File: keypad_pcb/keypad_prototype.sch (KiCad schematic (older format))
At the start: 31 parts, among them U1 KEYPAD_OVERLAY

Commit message: New keypad PCB
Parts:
- C1, C2, C3, C4, C5, C6, GREEN1, RED1: footprint Buttons_Switches_SMD:SW_SPST_EVQPE1 -> footprints:SW_SPST_EVQPE1
- OPTION1, PHOTO1, PHOTO2, VOL_DOWN1, VOL_UP1: footprint Buttons_Switches_SMD:SW_SPST_EVQP7C -> footprints:SW_SPST_EVQP7C
- U1: footprint keypad_overlay:KEYPAD_OVERLAY -> (none)
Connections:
- no-connect marks 2 -> 7
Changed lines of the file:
@@
 LIBS:valves
 LIBS:keypad_overlay
-LIBS:ab2_input_devices
 LIBS:keypad_prototype-cache
 EELAYER 25 0
@@
 $EndDescr
 $Comp
-L KEYPAD_OVERLAY U1
-U 1 1 58471DAF
-P 3650 2100
-F 0 "U1" H 3100 1450 60  0000 C CNN
-F 1 "KEYPAD_OVERLAY" H 3450 2500 60  0000 C CNN
-F 2 "keypad_overlay:KEYPAD_OVERLAY" H 3650 2100 60  0001 C CNN
-F 3 "" H 3650 2100 60  0001 C CNN
-	1    3650 2100
-	1    0    0    -1
-$EndComp
-$Comp
 L AB2_SWITCH_MOMENTARY VOL_DOWN1
 U 1 1 58471E29
@@
 F 0 "VOL_DOWN1" H 2650 3450 60  0000 C CNN
 F 1 "AB2_SWITCH_MOMENTARY" H 2650 3650 60  0001 C CNN
-F 2 "Buttons_Switches_SMD:SW_SPST_EVQP7C" H 2650 3500 60  0001 C CNN
+F 2 "footprints:SW_SPST_EVQP7C" H 2650 3500 60  0001 C CNN
 F 3 "" H 2650 3500 60  0000 C CNN
 	1    2650 3500
@@
 F 0 "VOL_UP1" H 3200 3450 60  0000 C CNN
 F 1 "AB2_SWITCH_MOMENTARY" H 3200 3650 60  0001 C CNN
-F 2 "Buttons_Switches_SMD:SW_SPST_EVQP7C" H 3200 3500 60  0001 C CNN
+F 2 "footprints:SW_SPST_EVQP7C" H 3200 3500 60  0001 C CNN
 F 3 "" H 3200 3500 60  0000 C CNN
 	1    3200 3500
@@
 F 0 "C1" H 3750 3450 60  0000 C CNN
 F 1 "AB2_SWITCH_MOMENTARY" H 3750 3650 60  0001 C CNN
-F 2 "Buttons_Switches_SMD:SW_SPST_EVQPE1" H 3750 3500 60  0001 C CNN
+F 2 "footprints:SW_SPST_EVQPE1" H 3750 3500 60  0001 C CNN
 F 3 "" H 3750 3500 60  0000 C CNN
 	1    3750 3500
@@
 F 0 "C2" H 4850 3450 60  0000 C CNN
 F 1 "AB2_SWITCH_MOMENTARY" H 4850 3650 60  0001 C CNN
-F 2 "Buttons_Switches_SMD:SW_SPST_EVQPE1" H 4850 3500 60  0001 C CNN
+F 2 "footprints:SW_SPST_EVQPE1" H 4850 3500 60  0001 C CNN
 F 3 "" H 4850 3500 60  0000 C CNN
 	1    4850 3500
@@
 F 0 "GREEN1" H 2650 3800 60  0000 C CNN
 F 1 "AB2_SWITCH_MOMENTARY" H 2650 4000 60  0001 C CNN
-F 2 "Buttons_Switches_SMD:SW_SPST_EVQPE1" H 2650 3850 60  0001 C CNN
+F 2 "footprints:SW_SPST_EVQPE1" H 2650 3850 60  0001 C CNN
 F 3 "" H 2650 3850 60  0000 C CNN
 	1    2650 3850
@@
 F 0 "RED1" H 4850 3800 60  0000 C CNN
 F 1 "AB2_SWITCH_MOMENTARY" H 4850 4000 60  0001 C CNN
-F 2 "Buttons_Switches_SMD:SW_SPST_EVQPE1" H 4850 3850 60  0001 C CNN
+F 2 "footprints:SW_SPST_EVQPE1" H 4850 3850 60  0001 C CNN
 F 3 "" H 4850 3850 60  0000 C CNN
 	1    4850 3850
@@
 F 0 "C3" H 3200 4150 60  0000 C CNN
 F 1 "AB2_SWITCH_MOMENTARY" H 3200 4350 60  0001 C CNN
-F 2 "Buttons_Switches_SMD:SW_SPST_EVQPE1" H 3200 4200 60  0001 C CNN
+F 2 "footprints:SW_SPST_EVQPE1" H 3200 4200 60  0001 C CNN
 F 3 "" H 3200 4200 60  0000 C CNN
 	1    3200 4200
@@
 F 0 "C4" H 4300 4150 60  0000 C CNN
 F 1 "AB2_SWITCH_MOMENTARY" H 4300 4350 60  0001 C CNN
-F 2 "Buttons_Switches_SMD:SW_SPST_EVQPE1" H 4300 4200 60  0001 C CNN
+F 2 "footprints:SW_SPST_EVQPE1" H 4300 4200 60  0001 C CNN
 F 3 "" H 4300 4200 60  0000 C CNN
 	1    4300 4200
@@
 F 0 "OPTION1" H 2650 4800 60  0000 C CNN
 F 1 "AB2_SWITCH_MOMENTARY" H 2650 5000 60  0001 C CNN
-F 2 "Buttons_Switches_SMD:SW_SPST_EVQP7C" H 2650 4850 60  0001 C CNN
+F 2 "footprints:SW_SPST_EVQP7C" H 2650 4850 60  0001 C CNN
 F 3 "" H 2650 4850 60  0000 C CNN
 	1    2650 4850
@@
 F 0 "PHOTO1" H 4850 4800 60  0000 C CNN
 F 1 "AB2_SWITCH_MOMENTARY" H 4850 5000 60  0001 C CNN
-F 2 "Buttons_Switches_SMD:SW_SPST_EVQP7C" H 4850 4850 60  0001 C CNN
+F 2 "footprints:SW_SPST_EVQP7C" H 4850 4850 60  0001 C CNN
 F 3 "" H 4850 4850 60  0000 C CNN
 	1    4850 4850
@@
 F 0 "C5" H 2650 5150 60  0000 C CNN
 F 1 "AB2_SWITCH_MOMENTARY" H 2650 5350 60  0001 C CNN
-F 2 "Buttons_Switches_SMD:SW_SPST_EVQPE1" H 2650 5200 60  0001 C CNN
+F 2 "footprints:SW_SPST_EVQPE1" H 2650 5200 60  0001 C CNN
 F 3 "" H 2650 5200 60  0000 C CNN
 	1    2650 5200
@@
 F 0 "C6" H 4300 5150 60  0000 C CNN
 F 1 "AB2_SWITCH_MOMENTARY" H 4300 5350 60  0001 C CNN
-F 2 "Buttons_Switches_SMD:SW_SPST_EVQPE1" H 4300 5200 60  0001 C CNN
+F 2 "footprints:SW_SPST_EVQPE1" H 4300 5200 60  0001 C CNN
 F 3 "" H 4300 5200 60  0000 C CNN
 	1    4300 5200
@@
 F 0 "PHOTO2" H 4850 5150 60  0000 C CNN
 F 1 "AB2_SWITCH_MOMENTARY" H 4850 5350 60  0001 C CNN
-F 2 "Buttons_Switches_SMD:SW_SPST_EVQP7C" H 4850 5200 60  0001 C CNN
+F 2 "footprints:SW_SPST_EVQP7C" H 4850 5200 60  0001 C CNN
 F 3 "" H 4850 5200 60  0000 C CNN
 	1    4850 5200
@@
 NoConn ~ 2850 2450
 NoConn ~ 2850 2550
+$Comp
+L KEYPAD_OVERLAY U1
+U 1 1 58866251
+P 3650 2100
+F 0 "U1" H 3100 1450 60  0000 C CNN
+F 1 "KEYPAD_OVERLAY" H 3450 2500 60  0000 C CNN
+F 2 "" H 3650 2100 60  0001 C CNN
+F 3 "" H 3650 2100 60  0001 C CNN
+	1    3650 2100
+	1    0    0    -1
+$EndComp
+NoConn ~ 3350 2850
+NoConn ~ 3450 2850
+NoConn ~ 3550 2850
+NoConn ~ 3650 2850
+NoConn ~ 3750 2850
 $EndSCHEMATC

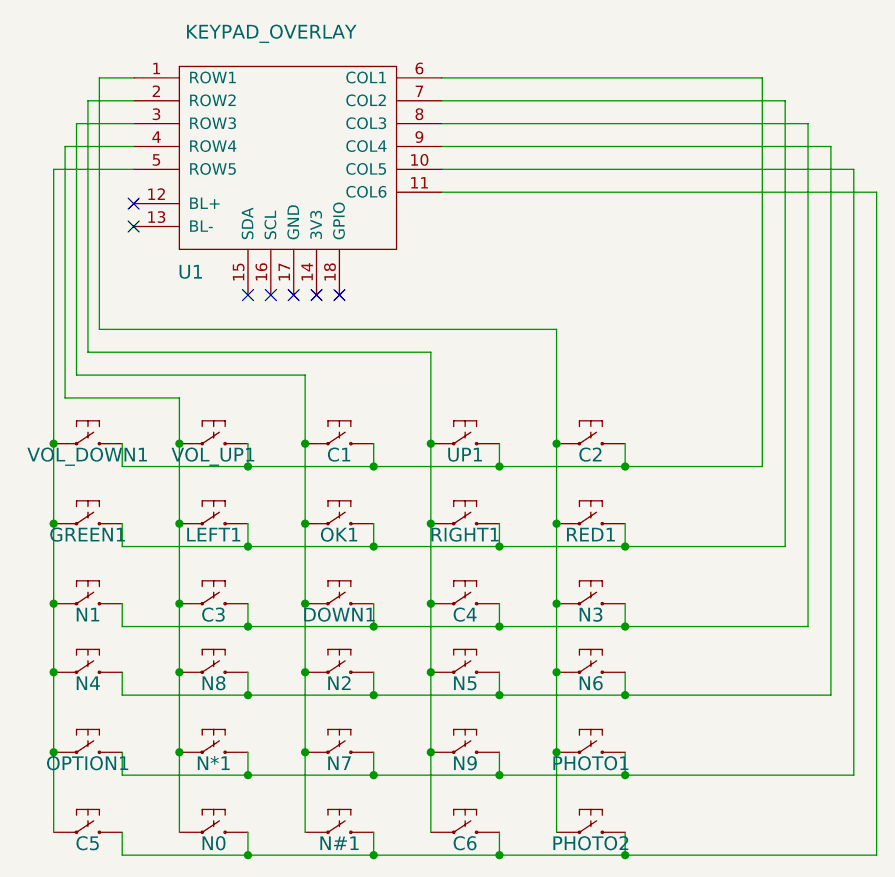
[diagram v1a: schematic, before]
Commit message: Silkscreen additions for keypad board
-Notes on soldering
-Tips for soldering
-Pin names
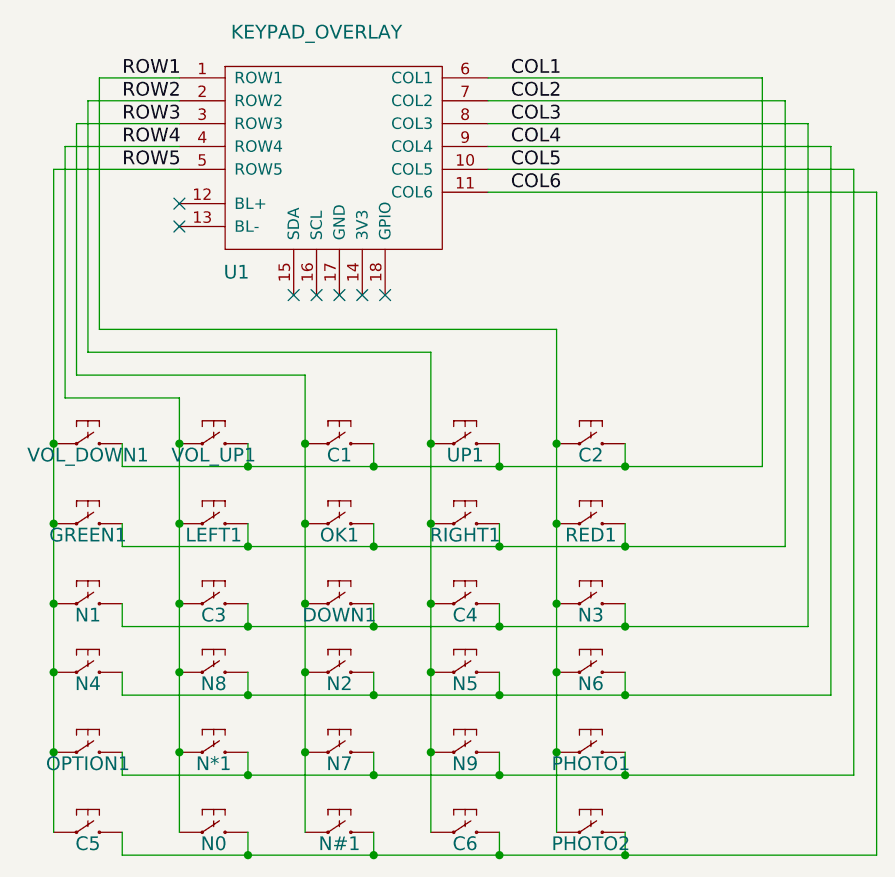
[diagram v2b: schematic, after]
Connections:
- net ROW5: now reaches C5.1, GREEN1.1, N1.1, N4.1, OPTION1.1, U1.5 (ROW5), VOL_DOWN1.1
- net COL1: now reaches C1.2, C2.2, U1.6 (COL1), UP1.2, VOL_DOWN1.2, VOL_UP1.2
- net ROW4: now reaches C3.1, LEFT1.1, N*1.1, N0.1, N8.1, U1.4 (ROW4), VOL_UP1.1
- net ROW3: now reaches C1.1, DOWN1.1, N#1.1, N2.1, N7.1, OK1.1, U1.3 (ROW3)
- net ROW2: now reaches C4.1, C6.1, N5.1, N9.1, RIGHT1.1, U1.2 (ROW2), UP1.1
- net ROW1: now reaches C2.1, N3.1, N6.1, PHOTO1.1, PHOTO2.1, RED1.1, U1.1 (ROW1)
- net COL2: now reaches GREEN1.2, LEFT1.2, OK1.2, RED1.2, RIGHT1.2, U1.7 (COL2)
- net COL3: now reaches C3.2, C4.2, DOWN1.2, N1.2, N3.2, U1.8 (COL3)
- net COL4: now reaches N2.2, N4.2, N5.2, N6.2, N8.2, U1.9 (COL4)
- net COL5: now reaches N*1.2, N7.2, N9.2, OPTION1.2, PHOTO1.2, U1.10 (COL5)
- net COL6: now reaches C5.2, C6.2, N#1.2, N0.2, PHOTO2.2, U1.11 (COL6)
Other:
- moved on the sheet: U1
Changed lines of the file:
@@
 	2500 2300 2500 5200
 Wire Wire Line
-	2700 1900 2850 1900
+	2700 1900 3050 1900
 Wire Wire Line
 	2700 1900 2700 3000
 Wire Wire Line
-	2850 2000 2650 2000
+	2650 2000 3050 2000
 Wire Wire Line
 	2650 2000 2650 3100
 Wire Wire Line
-	2850 2100 2600 2100
+	2600 2100 3050 2100
 Wire Wire Line
 	2600 2100 2600 3200
 Wire Wire Line
-	2850 2200 2550 2200
+	2550 2200 3050 2200
 Wire Wire Line
 	2550 2200 2550 3300
 Wire Wire Line
-	2850 2300 2500 2300
+	2500 2300 3050 2300
 Wire Wire Line
-	4200 2400 6100 2400
-Wire Wire Line
-	6100 2400 6100 5300
+	6100 5300 6100 2400
 Wire Wire Line
 	6000 4950 6000 2300
 Wire Wire Line
-	6000 2300 4200 2300
-Wire Wire Line
-	4200 2200 5900 2200
-Wire Wire Line
-	5900 2200 5900 4600
+	5900 4600 5900 2200
 Wire Wire Line
 	5800 4300 5800 2100
 Wire Wire Line
-	5800 2100 4200 2100
-Wire Wire Line
-	4200 2000 5700 2000
-Wire Wire Line
-	5700 2000 5700 3950
+	5700 3950 5700 2000
 Wire Wire Line
 	5600 3600 5600 1900
-Wire Wire Line
-	5600 1900 4200 1900
-NoConn ~ 2850 2450
-NoConn ~ 2850 2550
+NoConn ~ 3050 2450
+NoConn ~ 3050 2550
 $Comp
 L KEYPAD_OVERLAY U1
 U 1 1 58866251
-P 3650 2100
-F 0 "U1" H 3100 1450 60  0000 C CNN
-F 1 "KEYPAD_OVERLAY" H 3450 2500 60  0000 C CNN
-F 2 "" H 3650 2100 60  0001 C CNN
-F 3 "" H 3650 2100 60  0001 C CNN
-	1    3650 2100
+P 3850 2100
+F 0 "U1" H 3300 1450 60  0000 C CNN
+F 1 "KEYPAD_OVERLAY" H 3650 2500 60  0000 C CNN
+F 2 "" H 3850 2100 60  0001 C CNN
+F 3 "" H 3850 2100 60  0001 C CNN
+	1    3850 2100
 	1    0    0    -1
 $EndComp
-NoConn ~ 3350 2850
-NoConn ~ 3450 2850
+NoConn ~ 3950 2850
+NoConn ~ 3850 2850
 NoConn ~ 3550 2850
 NoConn ~ 3650 2850
 NoConn ~ 3750 2850
+Text Label 4500 1900 0    60   ~ 0
+COL1
+Text Label 4500 2000 0    60   ~ 0
+COL2
+Text Label 4500 2100 0    60   ~ 0
+COL3
+Text Label 4500 2200 0    60   ~ 0
+COL4
+Text Label 4500 2300 0    60   ~ 0
+COL5
+Text Label 4500 2400 0    60   ~ 0
+COL6
+Wire Wire Line
+	5600 1900 4400 1900
+Wire Wire Line
+	5700 2000 4400 2000
+Wire Wire Line
+	5800 2100 4400 2100
+Wire Wire Line
+	5900 2200 4400 2200
+Wire Wire Line
+	6000 2300 4400 2300
+Wire Wire Line
+	6100 2400 4400 2400
+Text Label 2800 1900 0    60   ~ 0
+ROW1
+Text Label 2800 2000 0    60   ~ 0
+ROW2
+Text Label 2800 2100 0    60   ~ 0
+ROW3
+Text Label 2800 2200 0    60   ~ 0
+ROW4
+Text Label 2800 2300 0    60   ~ 0
+ROW5
 $EndSCHEMATC
